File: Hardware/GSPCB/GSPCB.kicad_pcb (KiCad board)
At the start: 2 copper layers, 78.4 x 139.6 mm, 38 parts, among them J2 Conn_01x02_Socket, U4 LD39200PU33R

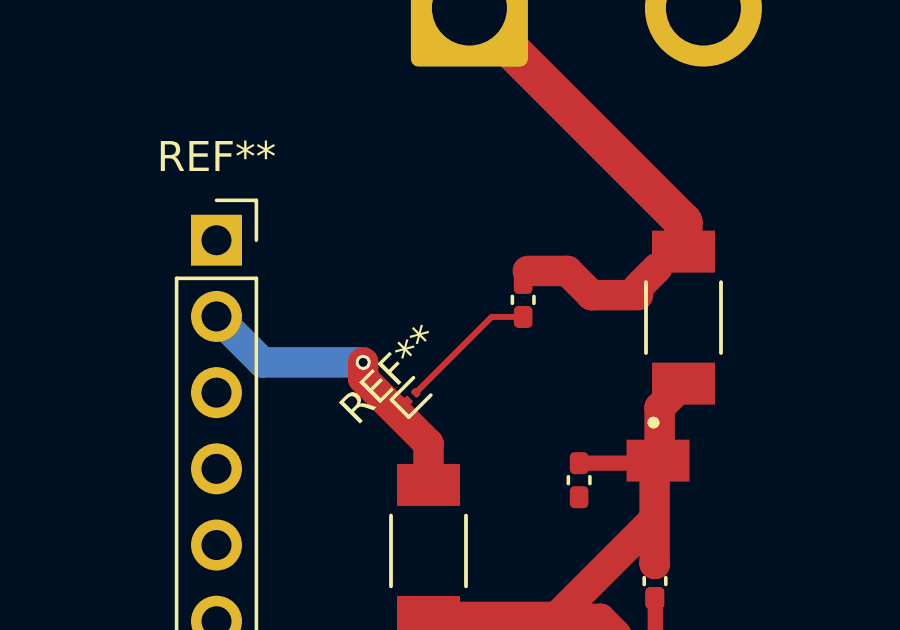
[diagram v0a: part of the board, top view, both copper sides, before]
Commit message: Quick touchups and final review for ordering, needs BoM confirmation
- Rerouted a couple signal lines on bottom layer for spacing and groundplane placement
- Touched up a few copper pour boundaries for simplified component placement
- Added more silkscreen labels and aligned with components, including I2C port pinout
- Standardized (larger) vias for JLCPCB ordering
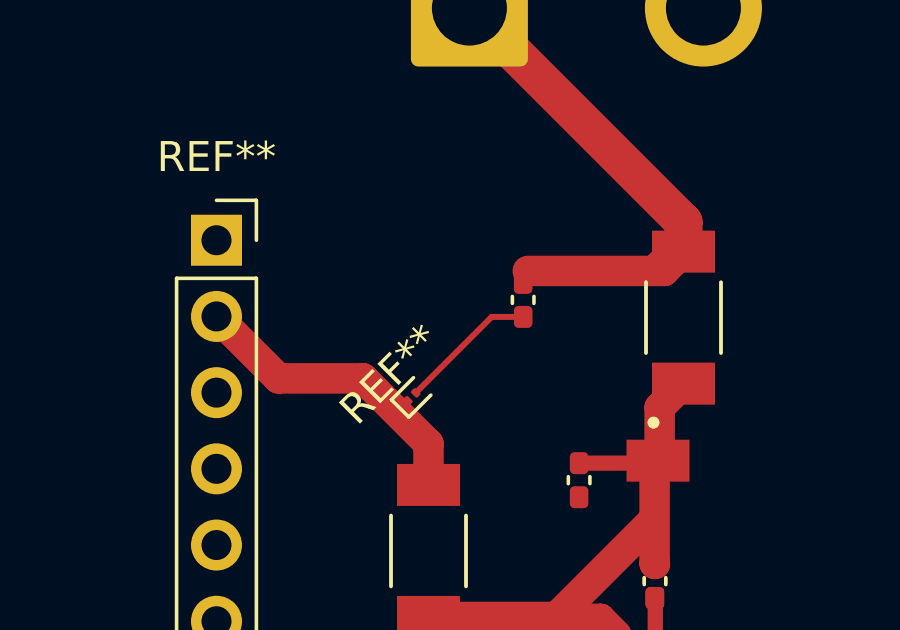
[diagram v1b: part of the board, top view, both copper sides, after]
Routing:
- net /VBATT: track 16.3 -> 17.6 mm
- net /Power Management/VBUS: track 10.8 -> 10.4 mm, vias 1 -> 0
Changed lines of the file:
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@@
 			(keep_text_aligned yes)
 		)
-		(gr_text "0.9409"
+		(gr_text "23.9"
 			(at 86.9196 133.7256 90)
 			(layer "F.Cu")
@@
 			(keep_text_aligned yes)
 		)
-		(gr_text "0.1589"
+		(gr_text "4.036"
 			(at 121.906 186.387 0)
 			(layer "Dwgs.User")
@@
 			(keep_text_aligned yes)
 		)
-		(gr_text "2.78"
+		(gr_text "70.612"
 			(at 84.582 40.0068 0)
 			(layer "Dwgs.User")
@@
 			(keep_text_aligned yes)
 		)
-		(gr_text "3.084"
+		(gr_text "78.3336"
 			(at 84.7318 34.5966 0)
 			(layer "Dwgs.User")
@@
 			(keep_text_aligned yes)
 		)
-		(gr_text "5.18"
+		(gr_text "131.572"
 			(at 39.462 113.792 90)
 			(layer "Dwgs.User")
@@
 			(keep_text_aligned yes)
 		)
-		(gr_text "5.4941"
+		(gr_text "139.5494"
 			(at 153.6604 113.801694 90)
 			(layer "Dwgs.User")
@@
 	)
 	(segment
+		(start 102.1521 101.5072)
+		(end 104.239 101.5072)
+		(width 0.2)
+		(layer "F.Cu")
+		(net 0)
+	)
+	(segment
 		(start 68.2818 55.1106)
 		(end 69.1362 55.965)
@@
 		(start 106.8947 97.7612)
 		(end 106.8647 97.7912)
-		(width 0.2)
-		(layer "F.Cu")
-		(net 0)
-	)
-	(segment
-		(start 102.1521 101.5072)
-		(end 104.239 101.5072)
 		(width 0.2)
 		(layer "F.Cu")
@@
 	)
 	(segment
+		(start 109.7395 154.1494)
+		(end 109.6005 154.2884)
+		(width 0.2)
+		(layer "F.Cu")
+		(net 0)
+	)
+	(segment
+		(start 66.4639 162.9606)
+		(end 70.6975 167.1942)
+		(width 0.2)
+		(layer "F.Cu")
+		(net 0)
+	)
+	(segment
+		(start 90.0404 62.6559)
+		(end 90.015 62.6813)
+		(width 0.2)
+		(layer "F.Cu")
+		(net 0)
+	)
+	(segment
+		(start 66.9913 139.0402)
+		(end 66.9913 140.3356)
+		(width 0.2)
+		(layer "F.Cu")
+		(net 0)
+	)
+	(segment
+		(start 57.2151 134.598)
+		(end 66.5127 143.8956)
+		(width 0.2)
+		(layer "F.Cu")
+		(net 0)
+	)
+	(segment
+		(start 100.9761 110.4912)
+		(end 102.4551 109.0122)
+		(width 0.2)
+		(layer "F.Cu")
+		(net 0)
+	)
+	(segment
+		(start 100.9761 85.3156)
+		(end 97.9008 85.3156)
+		(width 0.2)
+		(layer "F.Cu")
+		(net 0)
+	)
+	(segment
+		(start 87.6039 117.7632)
+		(end 54.8868 117.7632)
+		(width 0.2)
+		(layer "F.Cu")
+		(net 0)
+	)
+	(segment
+		(start 81.6467 92.7112)
+		(end 68.9171 92.7112)
+		(width 0.2)
+		(layer "F.Cu")
+		(net 0)
+	)
+	(segment
+		(start 79.8987 102.0792)
+		(end 67.9057 102.0792)
+		(width 0.2)
+		(layer "F.Cu")
+		(net 0)
+	)
+	(segment
+		(start 110.2115 105.1166)
+		(end 113.0556 105.1166)
+		(width 0.2)
+		(layer "F.Cu")
+		(net 0)
+	)
+	(segment
+		(start 86.9924 89.9493)
+		(end 87.0065 89.9634)
+		(width 0.2)
+		(layer "F.Cu")
+		(net 0)
+	)
+	(segment
+		(start 110.4424 125.7842)
+		(end 110.3582 125.8684)
+		(width 0.2)
+		(layer "F.Cu")
+		(net 0)
+	)
+	(segment
+		(start 68.2 132.098)
+		(end 51.0689 132.098)
+		(width 0.2)
+		(layer "F.Cu")
+		(net 0)
+	)
+	(segment
+		(start 50.9244 123.6306)
+		(end 49.5782 124.9768)
+		(width 0.2)
+		(layer "F.Cu")
+		(net 0)
+	)
+	(segment
+		(start 103.7451 110.2622)
+		(end 112.91 110.2622)
+		(width 0.2)
+		(layer "F.Cu")
+		(net 0)
+	)
+	(segment
+		(start 50.1878 111.4894)
+		(end 50.1878 109.6606)
+		(width 0.2)
+		(layer "F.Cu")
+		(net 0)
+	)
+	(segment
+		(start 51.0689 132.098)
+		(end 51.0119 132.041)
+		(width 0.2)
+		(layer "F.Cu")
+		(net 0)
+	)
+	(segment
 		(start 100.9761 100.3312)
 		(end 102.1521 101.5072)
-		(width 0.2)
-		(layer "F.Cu")
-		(net 0)
-	)
-	(segment
-		(start 109.7395 154.1494)
-		(end 109.6005 154.2884)
-		(width 0.2)
-		(layer "F.Cu")
-		(net 0)
-	)
-	(segment
-		(start 66.4639 162.9606)
-		(end 70.6975 167.1942)
-		(width 0.2)
-		(layer "F.Cu")
-		(net 0)
-	)
-	(segment
-		(start 90.0404 62.6559)
-		(end 90.015 62.6813)
-		(width 0.2)
-		(layer "F.Cu")
-		(net 0)
-	)
-	(segment
-		(start 66.9913 139.0402)
-		(end 66.9913 140.3356)
-		(width 0.2)
-		(layer "F.Cu")
-		(net 0)
-	)
-	(segment
-		(start 57.2151 134.598)
-		(end 66.5127 143.8956)
-		(width 0.2)
-		(layer "F.Cu")
-		(net 0)
-	)
-	(segment
-		(start 100.9761 110.4912)
-		(end 102.4551 109.0122)
-		(width 0.2)
-		(layer "F.Cu")
-		(net 0)
-	)
-	(segment
-		(start 100.9761 85.3156)
-		(end 97.9008 85.3156)
-		(width 0.2)
-		(layer "F.Cu")
-		(net 0)
-	)
-	(segment
-		(start 87.6039 117.7632)
-		(end 54.8868 117.7632)
-		(width 0.2)
-		(layer "F.Cu")
-		(net 0)
-	)
-	(segment
-		(start 81.6467 92.7112)
-		(end 68.9171 92.7112)
-		(width 0.2)
-		(layer "F.Cu")
-		(net 0)
-	)
-	(segment
-		(start 79.8987 102.0792)
-		(end 67.9057 102.0792)
-		(width 0.2)
-		(layer "F.Cu")
-		(net 0)
-	)
-	(segment
-		(start 110.2115 105.1166)
-		(end 113.0556 105.1166)
-		(width 0.2)
-		(layer "F.Cu")
-		(net 0)
-	)
-	(segment
-		(start 86.9924 89.9493)
-		(end 87.0065 89.9634)
-		(width 0.2)
-		(layer "F.Cu")
-		(net 0)
-	)
-	(segment
-		(start 110.4424 125.7842)
-		(end 110.3582 125.8684)
-		(width 0.2)
-		(layer "F.Cu")
-		(net 0)
-	)
-	(segment
-		(start 68.2 132.098)
-		(end 51.0689 132.098)
-		(width 0.2)
-		(layer "F.Cu")
-		(net 0)
-	)
-	(segment
-		(start 50.9244 123.6306)
-		(end 49.5782 124.9768)
-		(width 0.2)
-		(layer "F.Cu")
-		(net 0)
-	)
-	(segment
-		(start 103.7451 110.2622)
-		(end 112.91 110.2622)
-		(width 0.2)
-		(layer "F.Cu")
-		(net 0)
-	)
-	(segment
-		(start 50.1878 111.4894)
-		(end 50.1878 109.6606)
-		(width 0.2)
-		(layer "F.Cu")
-		(net 0)
-	)
-	(segment
-		(start 51.0689 132.098)
-		(end 51.0119 132.041)
 		(width 0.2)
 		(layer "F.Cu")
@@
 	)
 	(segment
-		(start 115.0279 66.33695)
-		(end 115.0279 66.60195)
-		(width 0.415)
+		(start 115.6704 65.69445)
+		(end 116.2143 65.15055)
+		(width 1.016)
+		(layer "F.Cu")
+		(net 4)
+	)
+	(segment
+		(start 116.2143 65.15055)
+		(end 116.54315 65.15055)
+		(width 1.016)
 		(layer "F.Cu")
 		(net 4)
@@
 	)
 	(segment
-		(start 111.351 65.7948)
-		(end 112.6718 65.7948)
+		(start 115.8989 65.7948)
+		(end 111.351 65.7948)
 		(width 1.016)
 		(layer "F.Cu")
@@
 	)
 	(segment
-		(start 112.6718 65.7948)
-		(end 113.47895 66.60195)
-		(width 1.016)
-		(layer "F.Cu")
-		(net 4)
-	)
-	(segment
-		(start 113.47895 66.60195)
-		(end 115.0279 66.60195)
-		(width 1.016)
-		(layer "F.Cu")
-		(net 4)
-	)
-	(segment
-		(start 115.6704 65.69445)
-		(end 115.0279 66.33695)
+		(start 116.54315 65.15055)
+		(end 115.8989 65.7948)
 		(width 1.016)
 		(layer "F.Cu")
@@
 	(segment
 		(start 105.8646 69.3762)
-		(end 105.8646 68.8428)
+		(end 103.0411 69.3762)
+		(width 1.016)
+		(layer "F.Cu")
+		(net 8)
+	)
+	(segment
+		(start 108.04305 72.92785)
+		(end 108.04305 71.55465)
+		(width 1.016)
+		(layer "F.Cu")
+		(net 8)
+	)
+	(segment
+		(start 103.0411 69.3762)
+		(end 100.9761 67.3112)
 		(width 1.016)
 		(layer "F.Cu")
@@
 		(net 8)
 	)
-	(segment
-		(start 105.82435 68.88305)
-		(end 105.8646 68.8428)
-		(width 0.415)
-		(layer "F.Cu")
-		(net 8)
-	)
-	(segment
-		(start 108.04305 72.92785)
-		(end 108.04305 71.55465)
-		(width 1.016)
-		(layer "F.Cu")
-		(net 8)
-	)
-	(via
-		(at 105.8646 68.8428)
-		(size 0.5)
-		(drill 0.3)
-		(layers "F.Cu" "B.Cu")
-		(net 8)
-	)
-	(segment
-		(start 105.8646 68.8428)
-		(end 102.5077 68.8428)
-		(width 1.016)
-		(layer "B.Cu")
-		(net 8)
-	)
-	(segment
-		(start 102.5077 68.8428)
-		(end 100.9761 67.3112)
-		(width 1.016)
-		(layer "B.Cu")
-		(net 8)
-	)
